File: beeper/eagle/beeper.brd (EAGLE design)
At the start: 29.2 x 39.8 mm, 32 parts, among them J4 ICSP, T1 MMBT3904, U1 ATA6631, U2 ATMEGA328P, X1 16MHz

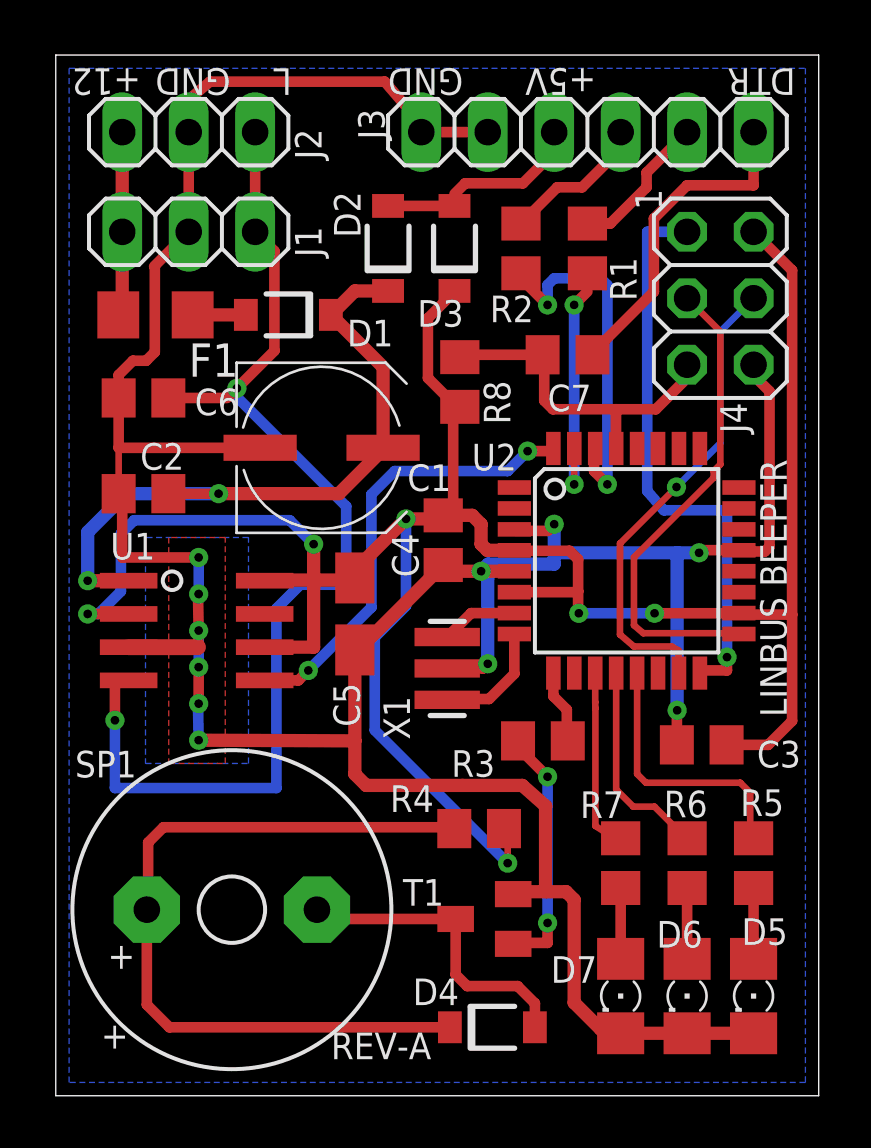
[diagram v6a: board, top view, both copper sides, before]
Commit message: Removed the third (status) led.
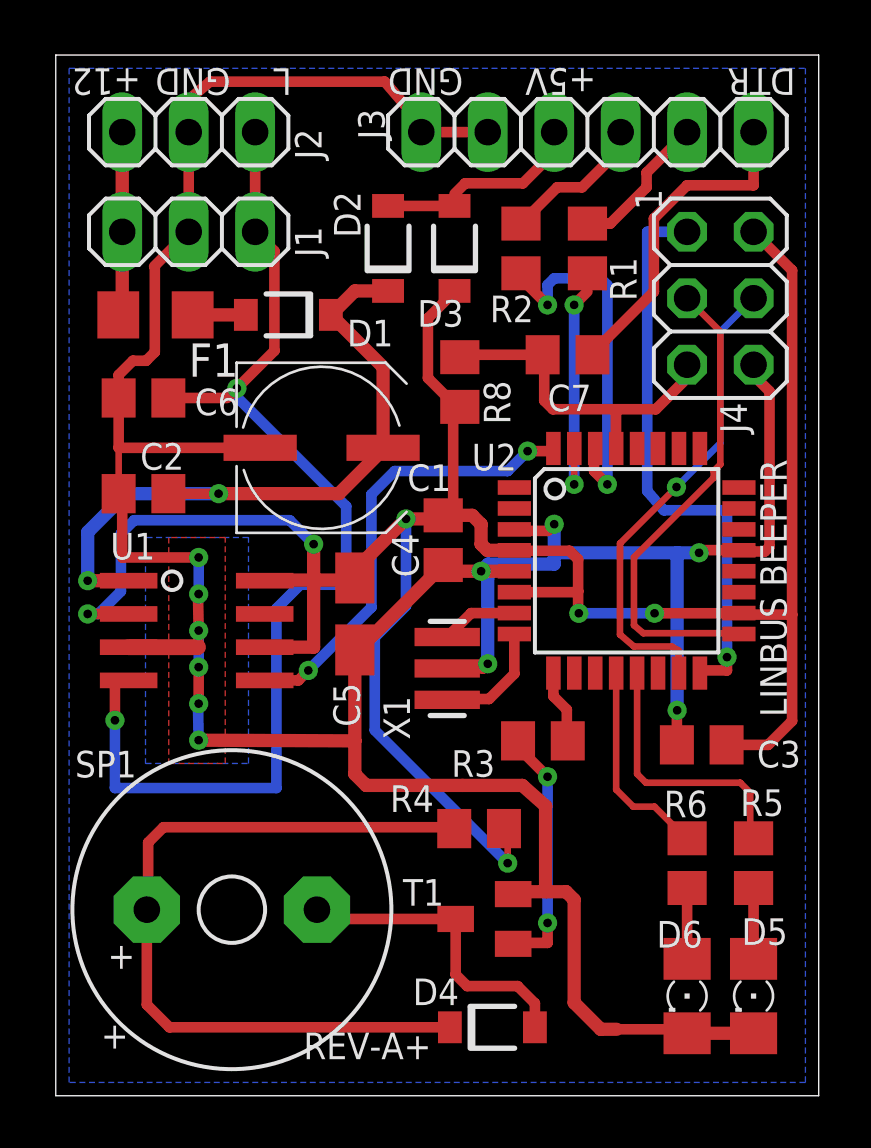
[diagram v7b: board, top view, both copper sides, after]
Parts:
- removed D7: GREEN, led:1206
- removed R7: 3.3K, rcl:R0805
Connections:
- removed net N$2: D7.A, R7.1
- removed net STATUS_LED: R7.2, U2.11
- net GND: no longer D7.C
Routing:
- net STATUS_LED: track 7.22 -> 0.00 mm
- net N$2: track 2.71 -> 0.00 mm
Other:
- board text added: "REV-A+"
- board text removed: "REV-A"
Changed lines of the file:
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@@
 <wire x1="0" y1="39.7764" x2="0" y2="0" width="0" layer="20"/>
 <text x="27.94" y="14.478" size="1.016" layer="21" rot="R90">LINBUS BEEPER</text>
-<text x="14.351" y="2.413" size="1.016" layer="21" rot="R180">REV-A</text>
+<text x="14.351" y="2.413" size="1.016" layer="21" rot="R180">REV-A+</text>
 <text x="3.2512" y="39.2684" size="1.016" layer="21" rot="SR180">+12</text>
 <text x="6.6802" y="39.2684" size="1.016" layer="21" rot="SR180">GND</text>
@@
 <attribute name="NAME" x="23.241" y="10.6426" size="1.016" layer="25"/>
 </element>
-<element name="R7" library="rcl" package="R0805" value="3.3K" x="21.59" y="8.89" smashed="yes" rot="R90">
-<attribute name="NAME" x="20.0406" y="10.6172" size="1.016" layer="25"/>
-</element>
 <element name="C6" library="rcl" package="C0805" value="220pF" x="3.3528" y="26.67" smashed="yes" rot="R180">
 <attribute name="NAME" x="6.985" y="27.0256" size="1.016" layer="25" rot="R180"/>
@@
 <element name="D6" library="led" package="1206" value="GREEN" x="24.13" y="3.81" smashed="yes" rot="R270">
 <attribute name="NAME" x="22.9616" y="5.6642" size="1.016" layer="25"/>
-</element>
-<element name="D7" library="led" package="1206" value="GREEN" x="21.59" y="3.81" smashed="yes" rot="R270">
-<attribute name="NAME" x="18.923" y="4.318" size="1.016" layer="25"/>
 </element>
 <element name="C1" library="rcl" package="UD-6,3X5,8_NICHICON" value="22uF 40V" x="10.16" y="24.765" smashed="yes">
@@
 <contactref element="D5" pad="C"/>
 <contactref element="D6" pad="C"/>
-<contactref element="D7" pad="C"/>
 <contactref element="C4" pad="2"/>
 <contactref element="C5" pad="-"/>
@@
 <via x="24.5872" y="20.7518" extent="1-16" drill="0.3302"/>
 <wire x1="17.483" y1="7.7064" x2="17.5744" y2="7.7978" width="0.4064" layer="1"/>
-<wire x1="21.59" y1="2.388" x2="24.13" y2="2.388" width="0.508" layer="1"/>
 <wire x1="26.67" y1="2.388" x2="24.13" y2="2.388" width="0.508" layer="1"/>
 <wire x1="18.7452" y1="7.7978" x2="18.7198" y2="7.8232" width="0.254" layer="1"/>
@@
 <wire x1="19.812" y1="7.493" x2="19.812" y2="3.556" width="0.508" layer="1"/>
 <wire x1="19.812" y1="3.556" x2="20.828" y2="2.54" width="0.508" layer="1"/>
-<wire x1="21.59" y1="2.388" x2="21.438" y2="2.54" width="0.508" layer="1"/>
 <wire x1="21.438" y1="2.54" x2="20.828" y2="2.54" width="0.508" layer="1"/>
 <wire x1="17.583" y1="21.59" x2="18.796" y2="21.59" width="0.4064" layer="1"/>
@@
 <vertex x="0.508" y="0.508"/>
 </polygon>
-</signal>
-<signal name="N$2">
-<contactref element="R7" pad="1"/>
-<contactref element="D7" pad="A"/>
-<wire x1="21.59" y1="7.94" x2="21.59" y2="5.232" width="0.4064" layer="1"/>
+<wire x1="21.438" y1="2.54" x2="24.13" y2="2.54" width="0.4064" layer="1"/>
+<wire x1="24.13" y1="2.54" x2="24.13" y2="2.388" width="0.4064" layer="1"/>
 </signal>
 <signal name="N$3">
@@
 <wire x1="21.4186" y1="11.703" x2="21.4186" y2="16.1544" width="0.254" layer="1"/>
 </signal>
-<signal name="STATUS_LED">
-<contactref element="R7" pad="2"/>
-<contactref element="U2" pad="11"/>
-<wire x1="20.6186" y1="16.1544" x2="20.6186" y2="15.043" width="0.254" layer="1"/>
-<wire x1="20.6186" y1="15.043" x2="20.6248" y2="14.8082" width="0.254" layer="1"/>
-<wire x1="20.6248" y1="14.8082" x2="20.6248" y2="10.3124" width="0.254" layer="1"/>
-<wire x1="20.6248" y1="10.3124" x2="20.9804" y2="10.0838" width="0.254" layer="1"/>
-<wire x1="21.082" y1="9.906" x2="21.59" y2="9.906" width="0.254" layer="1"/>
-<wire x1="21.082" y1="10.16" x2="21.082" y2="9.906" width="0.254" layer="1"/>
-<wire x1="21.59" y1="9.906" x2="21.59" y2="9.84" width="0.254" layer="1"/>
-<wire x1="21.082" y1="10.16" x2="20.9804" y2="10.0838" width="0.254" layer="1"/>
-</signal>
 <signal name="N$31">

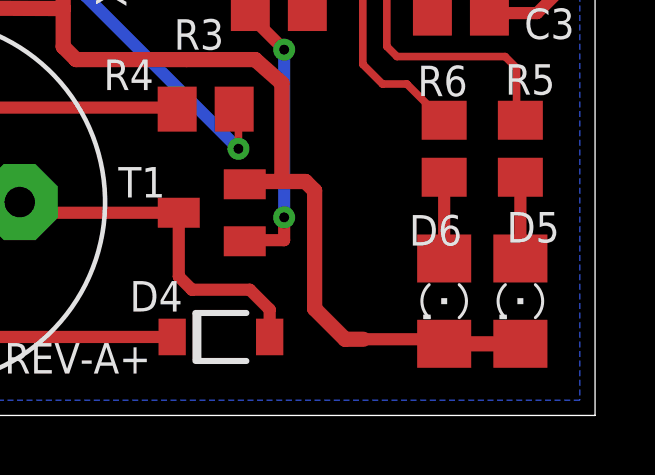
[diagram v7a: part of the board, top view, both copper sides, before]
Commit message: Created a clean beeper library. Moved majority of the componnents to the new library.
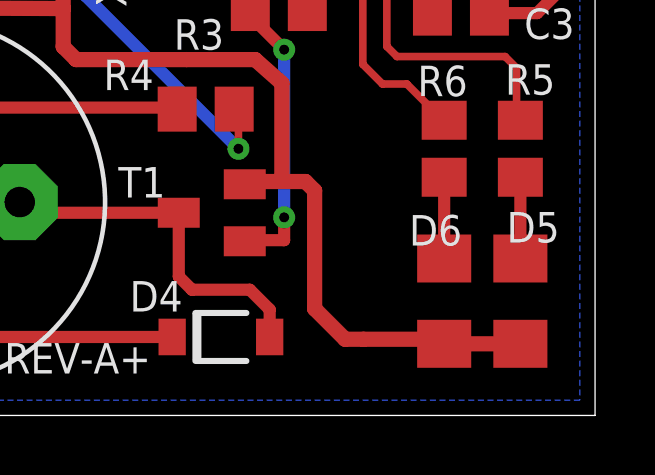
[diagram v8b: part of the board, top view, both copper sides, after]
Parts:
- C1: device rcl:UD-6,3X5,8_NICHICON -> beeper:UD-6,3X5,8_NICHICON
- C2, C3, C6, C7: device rcl:C0805 -> beeper:C0805
- C5: device rcl:A/3216-18R -> beeper:A/3216-18R
- D1, D2, D3, D4: device diode:SOD123FL -> beeper:SOD123FL
- D5, D6: device led:1206 -> beeper:1206
- J1, J2: device pinhead:1X03 -> beeper:1X03
- J3: device pinhead:1X06 -> beeper:1X06
- J4: device pinhead:2X03 -> beeper:2X03
- R1, R2, R4, R5, R6, R8: device rcl:R0805 -> beeper:R0805
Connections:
- net GND: now also D5.2, D6.2; no longer D5.C, D6.C
- net N$3: now also D6.1; no longer D6.A
- net N$4: now also D5.1; no longer D5.A
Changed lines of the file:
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@@
 <layers>
 <layer number="1" name="Top" color="4" fill="1" visible="yes" active="yes"/>
+<layer number="2" name="Route2" color="1" fill="3" visible="no" active="yes"/>
+<layer number="3" name="Route3" color="4" fill="3" visible="no" active="yes"/>
+<layer number="14" name="Route14" color="1" fill="6" visible="no" active="yes"/>
+<layer number="15" name="Route15" color="4" fill="6" visible="no" active="yes"/>
 <layer number="16" name="Bottom" color="1" fill="1" visible="yes" active="yes"/>
 <layer number="17" name="Pads" color="2" fill="1" visible="yes" active="yes"/>
@@
 </autorouter>
 <elements>
-<element name="R5" library="rcl" package="R0805" value="3.3K" x="26.67" y="8.89" smashed="yes" rot="R90">
+<element name="R5" library="beeper" package="R0805" value="3.3K" x="26.67" y="8.89" smashed="yes" rot="R90">
 <attribute name="NAME" x="26.162" y="10.6934" size="1.016" layer="25"/>
 </element>
-<element name="R6" library="rcl" package="R0805" value="3.3K" x="24.13" y="8.89" smashed="yes" rot="R90">
+<element name="R6" library="beeper" package="R0805" value="3.3K" x="24.13" y="8.89" smashed="yes" rot="R90">
 <attribute name="NAME" x="23.241" y="10.6426" size="1.016" layer="25"/>
 </element>
-<element name="C6" library="rcl" package="C0805" value="220pF" x="3.3528" y="26.67" smashed="yes" rot="R180">
+<element name="C6" library="beeper" package="C0805" value="220pF" x="3.3528" y="26.67" smashed="yes" rot="R180">
 <attribute name="NAME" x="6.985" y="27.0256" size="1.016" layer="25" rot="R180"/>
 </element>
-<element name="J1" library="pinhead" package="1X03" value="" x="5.08" y="33.02" smashed="yes">
+<element name="J1" library="beeper" package="1X03" value="" x="5.08" y="33.02" smashed="yes">
 <attribute name="NAME" x="10.16" y="32.0548" size="1.016" layer="25" ratio="10" rot="R90"/>
 <attribute name="VALUE" x="1.27" y="29.845" size="1.27" layer="27"/>
 </element>
-<element name="C3" library="rcl" package="C0805" value="0.1uF" x="24.6888" y="13.4112" smashed="yes" rot="R180">
+<element name="C3" library="beeper" package="C0805" value="0.1uF" x="24.6888" y="13.4112" smashed="yes" rot="R180">
 <attribute name="NAME" x="28.4734" y="13.5636" size="1.016" layer="25" rot="R180"/>
 </element>
-<element name="C7" library="rcl" package="C0805" value="0.1uF" x="19.558" y="28.321" smashed="yes" rot="R180">
+<element name="C7" library="beeper" package="C0805" value="0.1uF" x="19.558" y="28.321" smashed="yes" rot="R180">
 <attribute name="NAME" x="20.4724" y="27.178" size="1.016" layer="25" rot="R180"/>
 </element>
-<element name="R1" library="rcl" package="R0805" value="10k" x="20.32" y="32.385" smashed="yes" rot="R90">
+<element name="R1" library="beeper" package="R0805" value="10k" x="20.32" y="32.385" smashed="yes" rot="R90">
 <attribute name="NAME" x="22.1996" y="30.3784" size="1.016" layer="25" rot="R90"/>
 </element>
-<element name="R2" library="rcl" package="R0805" value="10k" x="17.78" y="32.385" smashed="yes" rot="R90">
+<element name="R2" library="beeper" package="R0805" value="10k" x="17.78" y="32.385" smashed="yes" rot="R90">
 <attribute name="NAME" x="18.2626" y="30.5816" size="1.016" layer="25" rot="R180"/>
 </element>
-<element name="J4" library="pinhead" package="2X03" value="ICSP" x="25.4" y="30.48" smashed="yes" rot="R270">
+<element name="J4" library="beeper" package="2X03" value="ICSP" x="25.4" y="30.48" smashed="yes" rot="R270">
 <attribute name="NAME" x="25.4" y="26.4922" size="1.016" layer="25" ratio="10" rot="R270"/>
 </element>
@@
 <attribute name="NAME" x="14.8336" y="8.2804" size="1.016" layer="25" rot="R180"/>
 </element>
-<element name="R4" library="rcl" package="R0805" value="0" x="16.1798" y="10.2108" smashed="yes">
+<element name="R4" library="beeper" package="R0805" value="0" x="16.1798" y="10.2108" smashed="yes">
 <attribute name="NAME" x="12.7762" y="10.8458" size="1.016" layer="25"/>
 </element>
-<element name="R8" library="rcl" package="R0805" value="10k" x="15.4432" y="27.2796" smashed="yes" rot="R270">
+<element name="R8" library="beeper" package="R0805" value="10k" x="15.4432" y="27.2796" smashed="yes" rot="R270">
 <attribute name="NAME" x="16.3576" y="27.3304" size="1.016" layer="25" rot="R270"/>
 </element>
@@
 <attribute name="NAME" x="2.0828" y="20.4978" size="1.016" layer="25"/>
 </element>
-<element name="J3" library="pinhead" package="1X06" value="" x="20.32" y="36.83" smashed="yes" rot="R180">
+<element name="J3" library="beeper" package="1X06" value="" x="20.32" y="36.83" smashed="yes" rot="R180">
 <attribute name="NAME" x="11.557" y="37.719" size="1.016" layer="25" ratio="10" rot="R270"/>
 <attribute name="VALUE" x="27.94" y="40.005" size="1.27" layer="27" rot="R180"/>
 </element>
-<element name="J2" library="pinhead" package="1X03" value="" x="5.08" y="36.83" smashed="yes">
+<element name="J2" library="beeper" package="1X03" value="" x="5.08" y="36.83" smashed="yes">
 <attribute name="NAME" x="10.16" y="35.7886" size="1.016" layer="25" ratio="10" rot="R90"/>
 <attribute name="VALUE" x="1.27" y="33.655" size="1.27" layer="27"/>
 </element>
-<element name="D1" library="diode" package="SOD123FL" value="MBR0540" x="8.89" y="29.845" smashed="yes" rot="R180">
+<element name="D1" library="beeper" package="SOD123FL" value="MBR0540" x="8.89" y="29.845" smashed="yes" rot="R180">
 <attribute name="NAME" x="12.8966" y="29.6578" size="1.016" layer="25" rot="R180"/>
 </element>
@@
 <attribute name="NAME" x="15.9004" y="23.9014" size="1.016" layer="25"/>
 </element>
-<element name="D2" library="diode" package="SOD123FL" value="MBR0540" x="12.7" y="32.385" smashed="yes" rot="R90">
+<element name="D2" library="beeper" package="SOD123FL" value="MBR0540" x="12.7" y="32.385" smashed="yes" rot="R90">
 <attribute name="NAME" x="11.6492" y="32.798" size="1.016" layer="25" rot="R90"/>
 </element>
-<element name="D3" library="diode" package="SOD123FL" value="MBR0540" x="15.24" y="32.385" smashed="yes" rot="R90">
+<element name="D3" library="beeper" package="SOD123FL" value="MBR0540" x="15.24" y="32.385" smashed="yes" rot="R90">
 <attribute name="NAME" x="15.5862" y="30.4104" size="1.016" layer="25" rot="R180"/>
 </element>
@@
 <attribute name="NAME" x="0.7366" y="12.1666" size="1.016" layer="25" ratio="10"/>
 </element>
-<element name="D4" library="diode" package="SOD123FL" value="MBR0540" x="16.6878" y="2.6162" smashed="yes">
+<element name="D4" library="beeper" package="SOD123FL" value="MBR0540" x="16.6878" y="2.6162" smashed="yes">
 <attribute name="NAME" x="13.6464" y="3.4638" size="1.016" layer="25"/>
 </element>
-<element name="D5" library="led" package="1206" value="RED" x="26.67" y="3.81" smashed="yes" rot="R270">
+<element name="D5" library="beeper" package="1206" value="RED" x="26.67" y="3.81" smashed="yes" rot="R270">
 <attribute name="NAME" x="26.2128" y="5.7658" size="1.016" layer="25"/>
 </element>
-<element name="D6" library="led" package="1206" value="GREEN" x="24.13" y="3.81" smashed="yes" rot="R270">
+<element name="D6" library="beeper" package="1206" value="GREEN" x="24.13" y="3.81" smashed="yes" rot="R270">
 <attribute name="NAME" x="22.9616" y="5.6642" size="1.016" layer="25"/>
 </element>
-<element name="C1" library="rcl" package="UD-6,3X5,8_NICHICON" value="22uF 40V" x="10.16" y="24.765" smashed="yes">
+<element name="C1" library="beeper" package="UD-6,3X5,8_NICHICON" value="22uF 40V" x="10.16" y="24.765" smashed="yes">
 <attribute name="NAME" x="13.4366" y="23.114" size="1.016" layer="25"/>
 </element>
-<element name="C2" library="rcl" package="C0805" value="0.1uF" x="3.3528" y="23.0124" smashed="yes" rot="R180">
+<element name="C2" library="beeper" package="C0805" value="0.1uF" x="3.3528" y="23.0124" smashed="yes" rot="R180">
 <attribute name="NAME" x="4.9022" y="24.9428" size="1.016" layer="25" rot="R180"/>
 </element>
-<element name="C5" library="rcl" package="A/3216-18R" value="10uF" x="11.43" y="18.415" smashed="yes" rot="R90">
+<element name="C5" library="beeper" package="A/3216-18R" value="10uF" x="11.43" y="18.415" smashed="yes" rot="R90">
 <attribute name="NAME" x="11.6238" y="14.1028" size="1.016" layer="25" rot="R90"/>
 </element>
@@
 <contactref element="T1" pad="E"/>
 <contactref element="X1" pad="2"/>
-<contactref element="D5" pad="C"/>
-<contactref element="D6" pad="C"/>
+<contactref element="D5" pad="2"/>
+<contactref element="D6" pad="2"/>
 <contactref element="C4" pad="2"/>
 <contactref element="C5" pad="-"/>
@@
 <vertex x="0.508" y="0.508"/>
 </polygon>
-<wire x1="21.438" y1="2.54" x2="24.13" y2="2.54" width="0.4064" layer="1"/>
+<wire x1="21.438" y1="2.54" x2="24.13" y2="2.54" width="0.508" layer="1"/>
 <wire x1="24.13" y1="2.54" x2="24.13" y2="2.388" width="0.4064" layer="1"/>
 </signal>
 <signal name="N$3">
 <contactref element="R6" pad="1"/>
-<contactref element="D6" pad="A"/>
+<contactref element="D6" pad="1"/>
 <wire x1="24.13" y1="7.94" x2="24.13" y2="5.232" width="0.4064" layer="1"/>
 </signal>
 <signal name="N$4">
 <contactref element="R5" pad="1"/>
-<contactref element="D5" pad="A"/>
+<contactref element="D5" pad="1"/>
 <wire x1="26.67" y1="7.94" x2="26.67" y2="5.232" width="0.4064" layer="1"/>
 </signal>
